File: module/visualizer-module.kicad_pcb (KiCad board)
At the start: 2 copper layers, 10 parts, among them J1 USB4110GFA

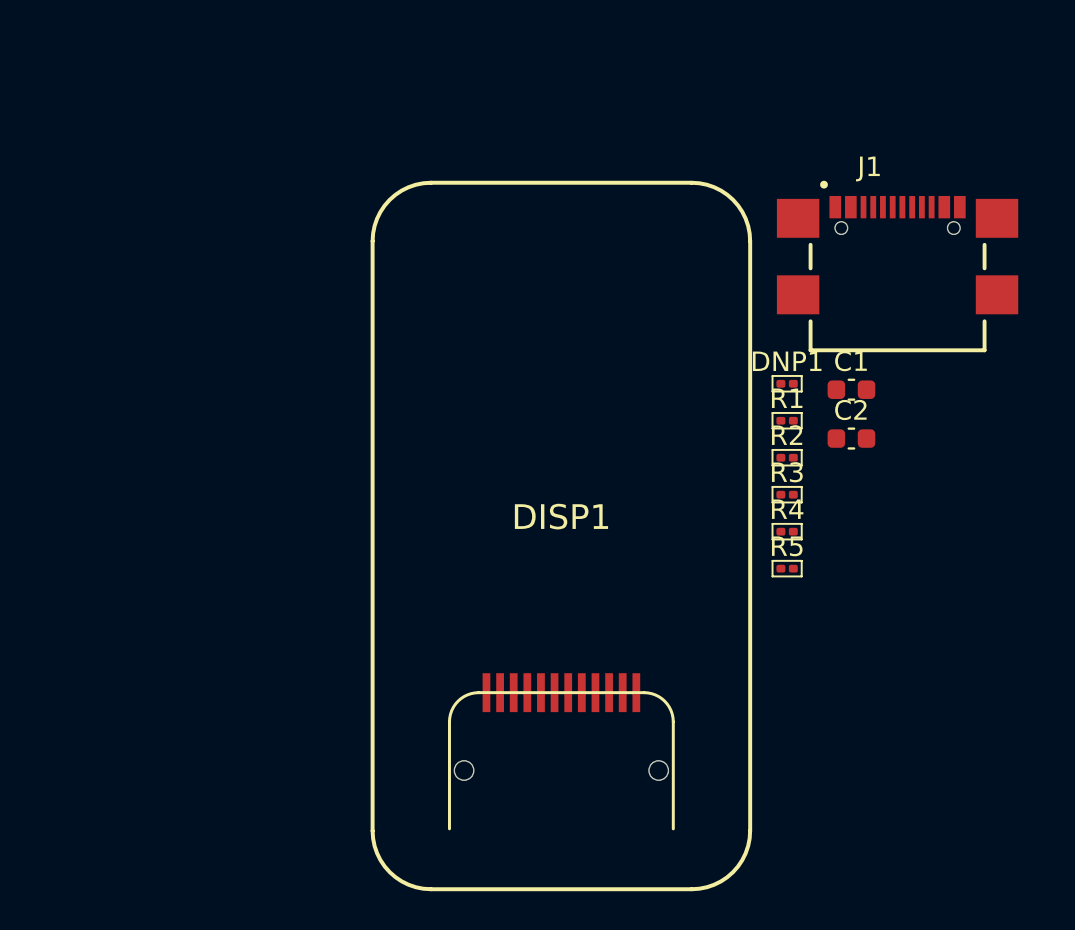
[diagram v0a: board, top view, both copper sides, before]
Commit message: Updated symbol and attached some models to some of the components
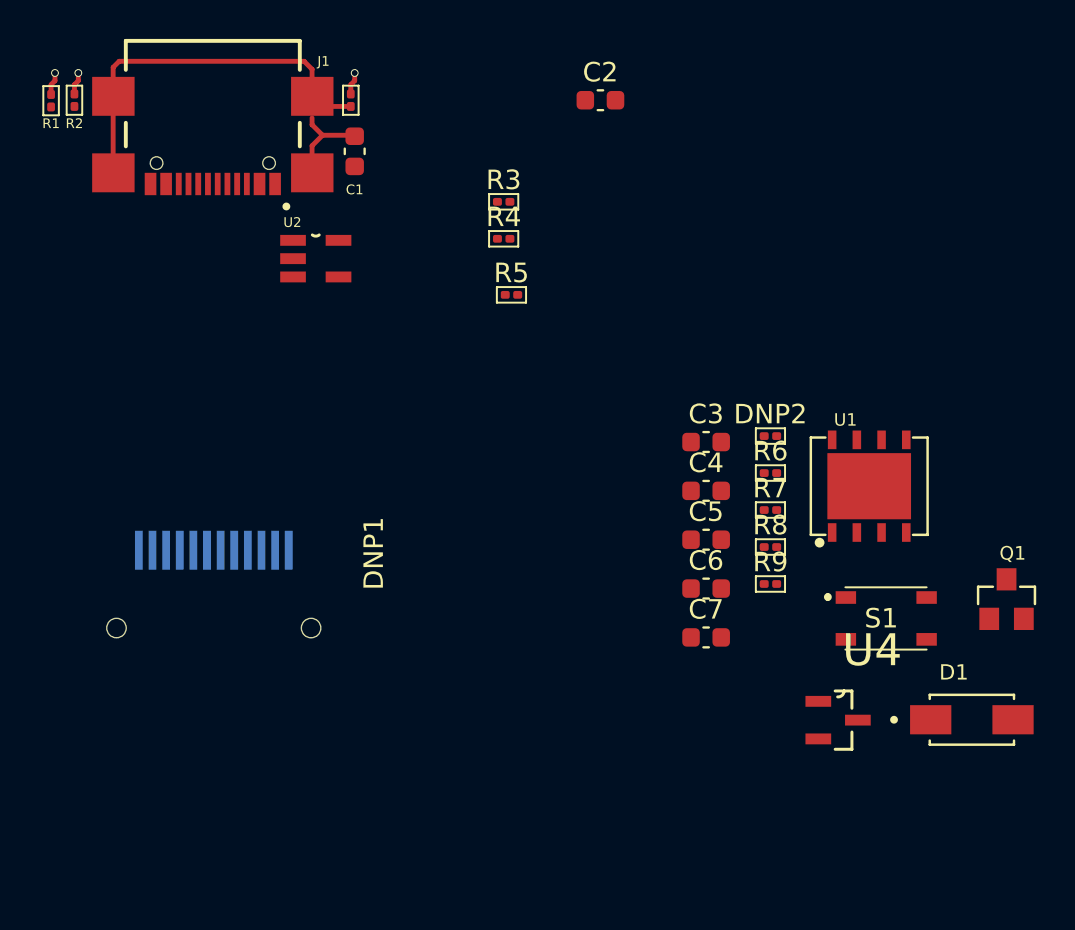
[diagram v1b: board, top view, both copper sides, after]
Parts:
- added C3: 0.1uF_0603_16V, Capacitor_SMD:C_0603_1608Metric, F.Cu at (111.7, 74.6)
- added C4: 0.1uF_0603_16V, Capacitor_SMD:C_0603_1608Metric, F.Cu at (111.7, 77.1)
- added C5: 0.1uF_0603_16V, Capacitor_SMD:C_0603_1608Metric, F.Cu at (111.7, 79.6)
- added C6: 0.1uF_0603_16V, Capacitor_SMD:C_0603_1608Metric, F.Cu at (111.7, 82.1)
- added C7: 0.1uF_0603_16V, Capacitor_SMD:C_0603_1608Metric, F.Cu at (111.7, 84.6)
- added D1: SS14, footprints:SS14, F.Cu at (125.3, 88.8)
- added DNP2: 10K_0603, PCM_Resistor_SMD_AKL:R_0201_0603Metric, F.Cu at (115.0, 74.3)
- added Q1: ~, footprints:S8050, F.Cu at (127.1, 82.6)
- added R6: 10K_0603, PCM_Resistor_SMD_AKL:R_0201_0603Metric, F.Cu at (115.0, 76.2)
- added R7: 10K_0603, PCM_Resistor_SMD_AKL:R_0201_0603Metric, F.Cu at (115.0, 78.1)
- added R8: 10K_0603, PCM_Resistor_SMD_AKL:R_0201_0603Metric, F.Cu at (115.0, 80.0)
- added R9: 10K_0603, PCM_Resistor_SMD_AKL:R_0201_0603Metric, F.Cu at (115.0, 81.9)
- added S1: PTS810SJK250SMTRLFS, footprints:PTS810SJG250SMTRLFS, F.Cu at (120.9, 83.6)
- added U1: W25Q128JVSIQ, footprints:W25Q128JVPIM, F.Cu at (120.0, 76.8)
- added U2: SPX3819M5-L, footprints:SPX3819M5-L, F.Cu at (91.6, 65.1)
- added U4: DMG3415U-7, footprints:DMG3415U-7, F.Cu at (118.4, 88.9)
- DISP1: moved to B.Cu
- moved R1 41.2 mm to (78.0, 57.0), turned to -90 degrees
- moved R2 41.0 mm to (79.2, 57.0), turned to -90 degrees
- moved J1 35.3 mm to (86.3, 60.2), turned to 180 degrees
- moved C1 28.3 mm to (93.6, 59.6), turned to -90 degrees
- moved DNP1 26.7 mm to (93.4, 57.0), turned to -90 degrees
- moved C2 21.6 mm to (106.2, 57.0)
- moved R3 20.9 mm to (101.3, 62.2)
- moved R4 20.9 mm to (101.3, 64.1)
- moved R5 20.0 mm to (101.7, 67.0)
- moved DISP1 19.3 mm to (86.4, 71.1), turned to 180 degrees
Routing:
- net /SH: track 0.00 -> 24.5 mm
- net GND: track 0.00 -> 3.51 mm, vias 0 -> 3
